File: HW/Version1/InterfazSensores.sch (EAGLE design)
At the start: 30 parts, among them IC1 LM2940, T1 BC846, T2 BC846, T3 BC846

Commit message: Placa finalizada
Revisada, lista para fabricar.
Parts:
- renumbered CENTRAL to J1, MAX485 to IC2, MICRO to IC3, SENSOR to J2, SV1 to BDM

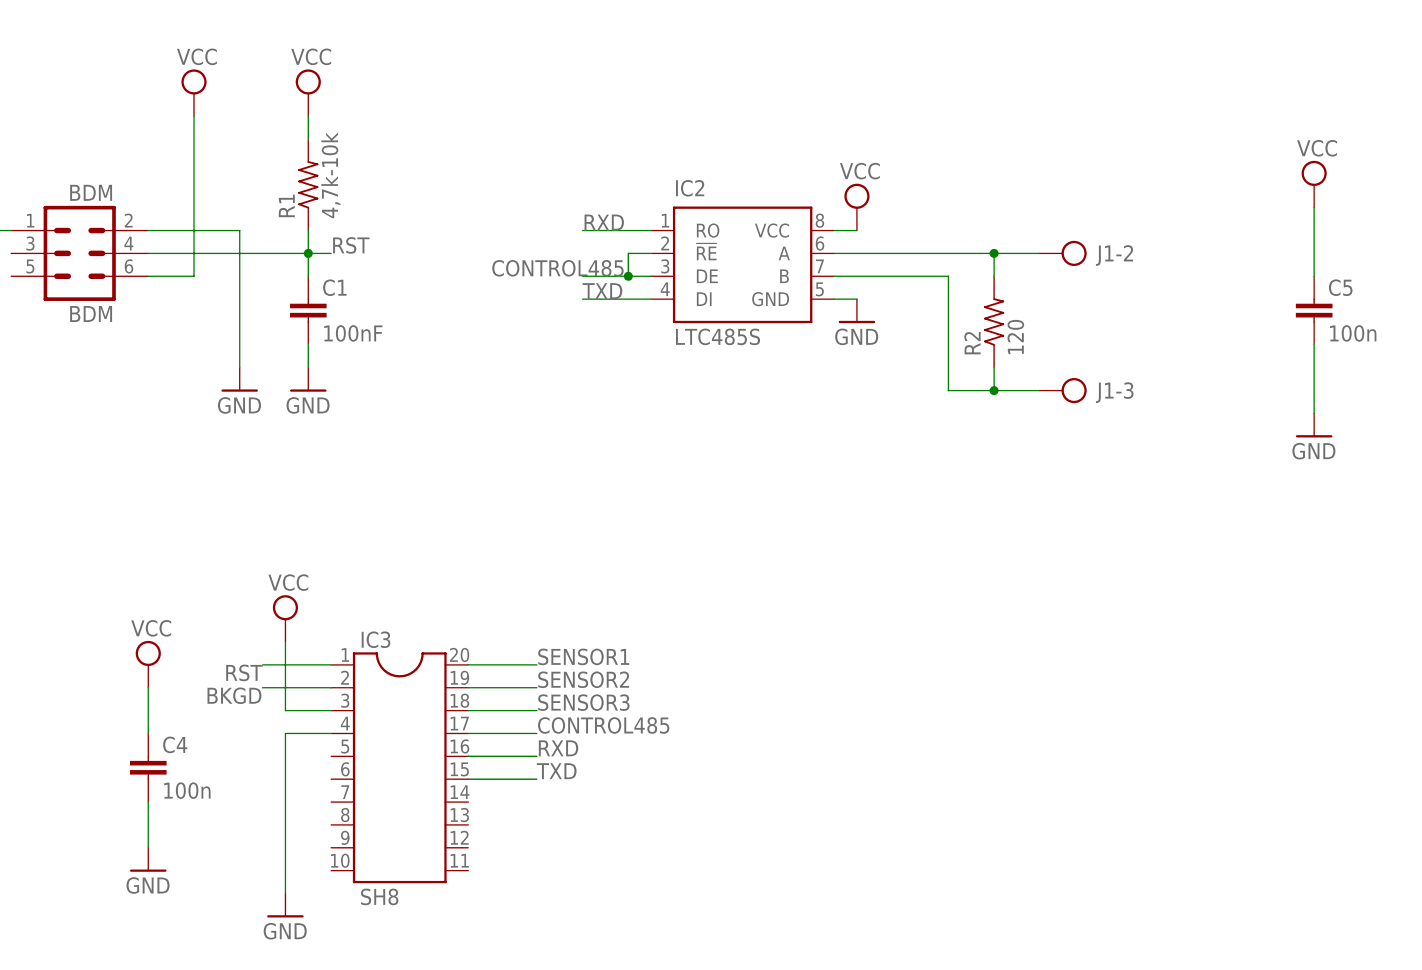
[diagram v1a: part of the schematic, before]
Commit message: Actualizo y agrego lista de materiales
Lista de materiales actualizada a travez del SCH
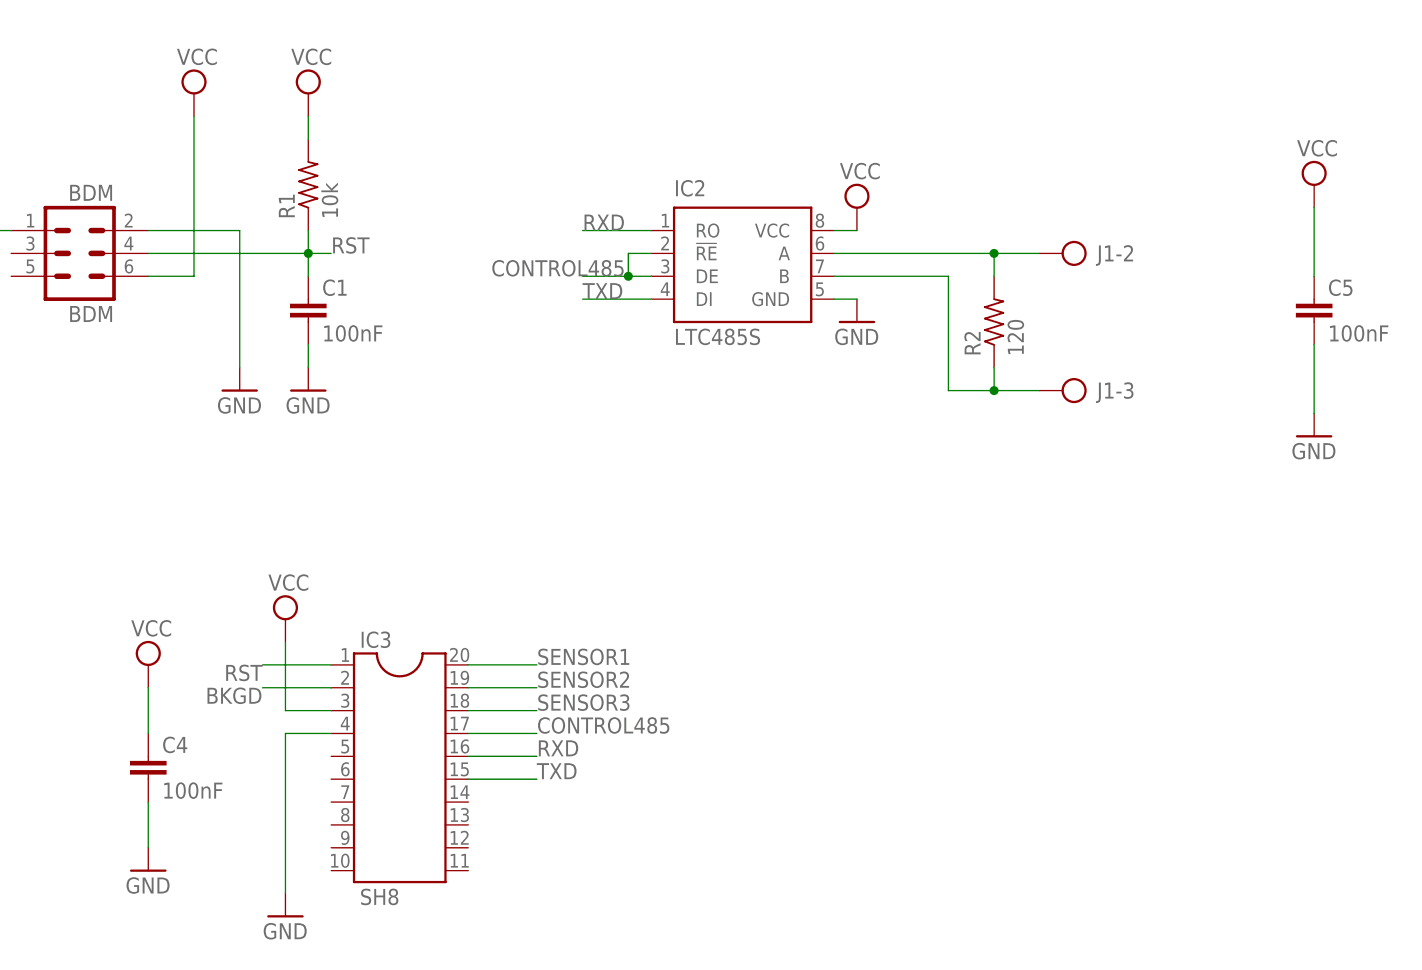
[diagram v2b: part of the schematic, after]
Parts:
- C4, C5: value 100n -> 100nF
- R1: value 4,7k-10k -> 10k
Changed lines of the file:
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@@
 <part name="SUPPLY4" library="supply2" deviceset="VCC" device=""/>
 <part name="GND5" library="supply1" deviceset="GND" device=""/>
-<part name="R1" library="resistor" deviceset="R-US_" device="R0805" value="4,7k-10k"/>
+<part name="R1" library="resistor" deviceset="R-US_" device="R0805" value="10k"/>
 <part name="C1" library="resistor" deviceset="C-EU" device="C0805" value="100nF"/>
 <part name="GND6" library="supply1" deviceset="GND" device=""/>
@@
 <part name="IC2" library="linear-technology" deviceset="LTC485" device="S"/>
 <part name="R2" library="resistor" deviceset="R-US_" device="R0805" value="120"/>
-<part name="C4" library="resistor" deviceset="C-EU" device="C0805" value="100n"/>
-<part name="C5" library="resistor" deviceset="C-EU" device="C0805" value="100n"/>
+<part name="C4" library="resistor" deviceset="C-EU" device="C0805" value="100nF"/>
+<part name="C5" library="resistor" deviceset="C-EU" device="C0805" value="100nF"/>
 <part name="SUPPLY6" library="supply2" deviceset="VCC" device=""/>
 <part name="GND7" library="supply1" deviceset="GND" device=""/>
